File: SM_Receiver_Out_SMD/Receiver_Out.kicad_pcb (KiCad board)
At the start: 2 copper layers, 83.2 x 71.4 mm, 47 parts, among them J1 String1, J2 String2, J3 String3, J4 String4, J5 OLED, J6 VIN_Voltage, J7 RJ45, J8 RJ45, SW1 ID, SW2 Terminators, SW3 User, SW4 RUN, U1 74AHCT1G125, U2 AMS1117-5.0, U3 AM26C32IN, U4 74AHCT1G125, U5 74AHCT1G125, U6 74AHCT1G125, U7 Pico

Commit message: working on BOM
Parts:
- added J10: SWD, Scotts:1x02_Horizontal_SMD, B.Cu at (63.6, 82.9)
- added J9: Debug, Connector_PinHeader_2.54mm:PinHeader_1x03_P2.54mm_Vertical, F.Cu at (70.0, 150.0)
- added R2: 100K, Resistor_SMD:R_0603_1608Metric_Pad0.98x0.95mm_HandSolder, F.Cu at (78.0, 139.0)
- added TP1: DATA1, TestPoint:TestPoint_Pad_D1.5mm, B.Cu at (64.7, 134.7)
- added TP2: DATA2, TestPoint:TestPoint_Pad_D1.5mm, B.Cu at (64.7, 132.1)
- added TP3: DATA3, TestPoint:TestPoint_Pad_D1.5mm, B.Cu at (64.7, 129.5)
- added TP4: DATA4, TestPoint:TestPoint_Pad_D1.5mm, B.Cu at (64.7, 127.0)
- added TP5: EN1, TestPoint:TestPoint_Pad_D1.5mm, B.Cu at (64.6, 109.2)
- added TP6: EN2, TestPoint:TestPoint_Pad_D1.5mm, B.Cu at (64.5, 106.7)
- added TP7: EN3, TestPoint:TestPoint_Pad_D1.5mm, B.Cu at (64.4, 104.2)
- added TP8: EN4, TestPoint:TestPoint_Pad_D1.5mm, B.Cu at (64.4, 101.6)
- moved REF** 3.70 mm to (53.5, 116.9)
- turned D4 to 180 degrees
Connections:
- R11 pad 1: Net-(D4-Pad2) -> Net-(D4-Pad1)
- U3 pad 12: GND -> DIFF_EN
- U7 pad 1: unconnected-(U7-Pad1) -> Net-(J9-Pad2)
- U7 pad 11: unconnected-(U7-Pad11) -> DIFF_EN
- U7 pad 2: unconnected-(U7-Pad2) -> Net-(J9-Pad1)
- U7 pad 41: unconnected-(U7-Pad41) -> /Micro/SWDCLK
- U7 pad 42: unconnected-(U7-Pad42) -> GND
- U7 pad 43: unconnected-(U7-Pad43) -> /Micro/SWDIO
- U7 pad 9: Net-(D4-Pad1) -> Net-(D4-Pad2)
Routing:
- net DIFF_EN: track 0.00 -> 39.1 mm, vias 0 -> 2
- net Net-(D4-Pad2): track 1.91 -> 26.3 mm
- net Net-(D4-Pad1): track 26.3 -> 1.91 mm
- net Net-(J9-Pad1): track 0.00 -> 14.6 mm
- net Net-(J9-Pad2): track 0.00 -> 12.5 mm
- net /Micro/SWDIO: track 0.00 -> 12.5 mm, vias 0 -> 1
- net /Micro/SWDCLK: track 0.00 -> 11.5 mm, vias 0 -> 1
- net EN3: track 10.8 -> 13.5 mm
- net EN4: track 8.43 -> 11.1 mm
- net EN2: track 8.62 -> 11.2 mm
- net EN1: track 9.27 -> 11.8 mm
- net OUT17: track 34.8 -> 37.3 mm
- net OUT18: track 43.9 -> 46.3 mm
- net OUT19: track 36.2 -> 38.6 mm
- net OUT20: track 46.7 -> 49.1 mm
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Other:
- board text added: "${TITLE} ${REVISION} By ${COMPANY}"
- board text added: "GP0"
- board text added: "GP1"
- board text added: "SWDCLK"
- board text added: "SWDIO"
- board text removed: "SM Receiver v1 By Scott Hanson"

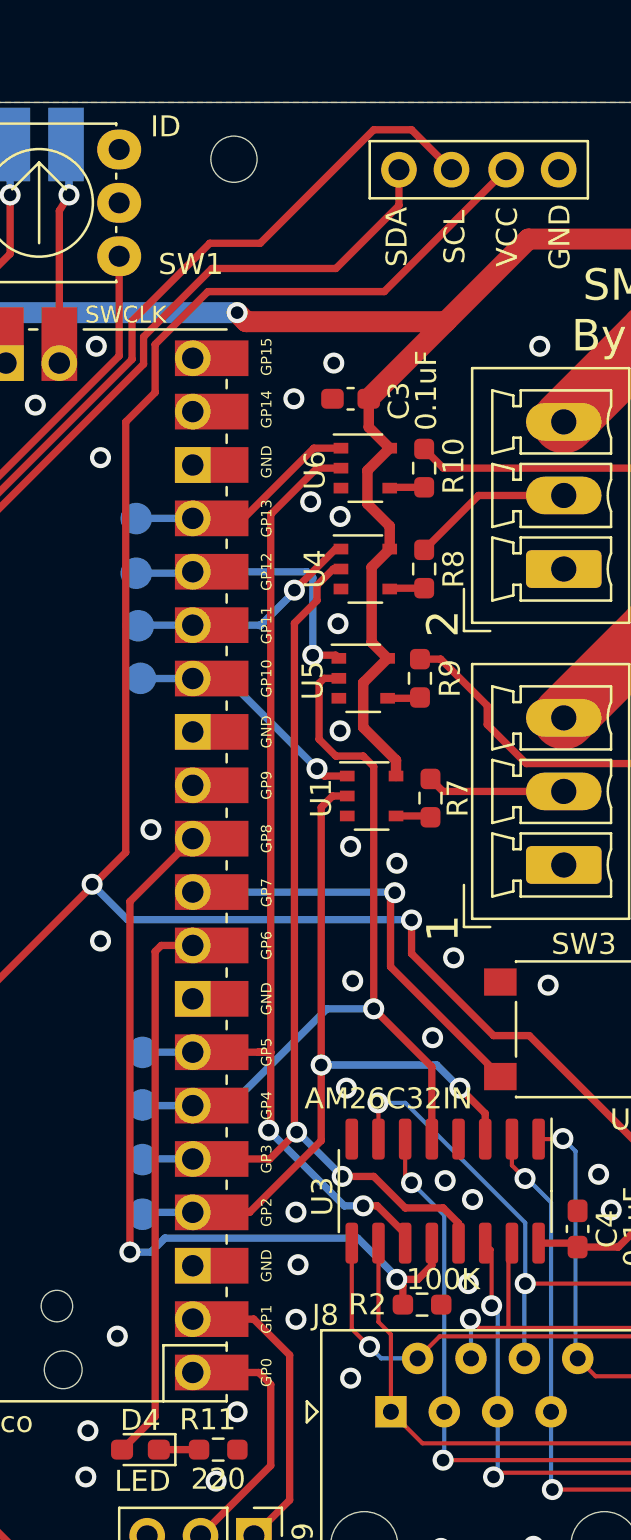
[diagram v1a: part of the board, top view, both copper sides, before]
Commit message: fixing I2C lines were backwards
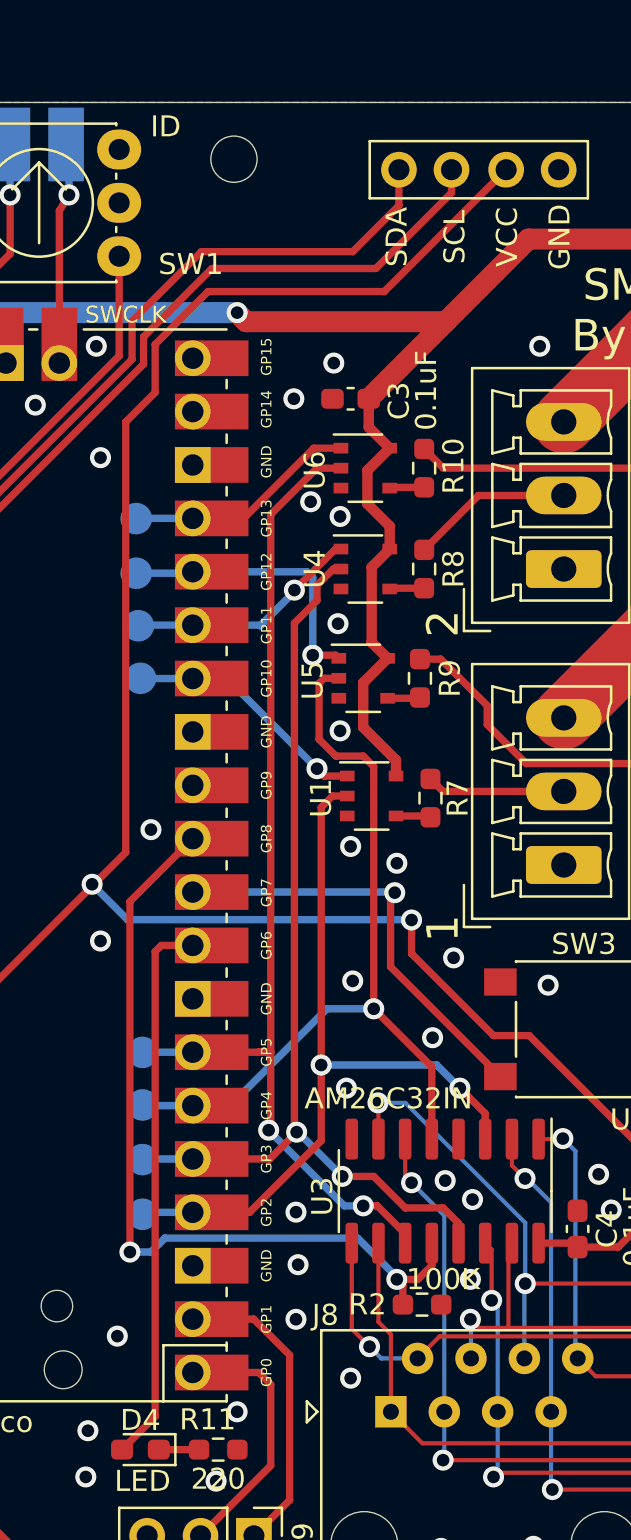
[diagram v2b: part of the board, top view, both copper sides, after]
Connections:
- J5 pad 1: Net-(J5-Pad1) -> /Micro/SDA
- J5 pad 2: Net-(J5-Pad2) -> /Micro/SCL
- U7 pad 31: Net-(J5-Pad2) -> /Micro/SDA
- U7 pad 32: Net-(J5-Pad1) -> /Micro/SCL
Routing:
- net /Micro/SCL: track 0.00 -> 53.9 mm
- net Net-(J5-Pad2): track 53.7 -> 0.00 mm
- net Net-(J5-Pad1): track 51.8 -> 0.00 mm
- net /Micro/SDA: track 0.00 -> 50.6 mm

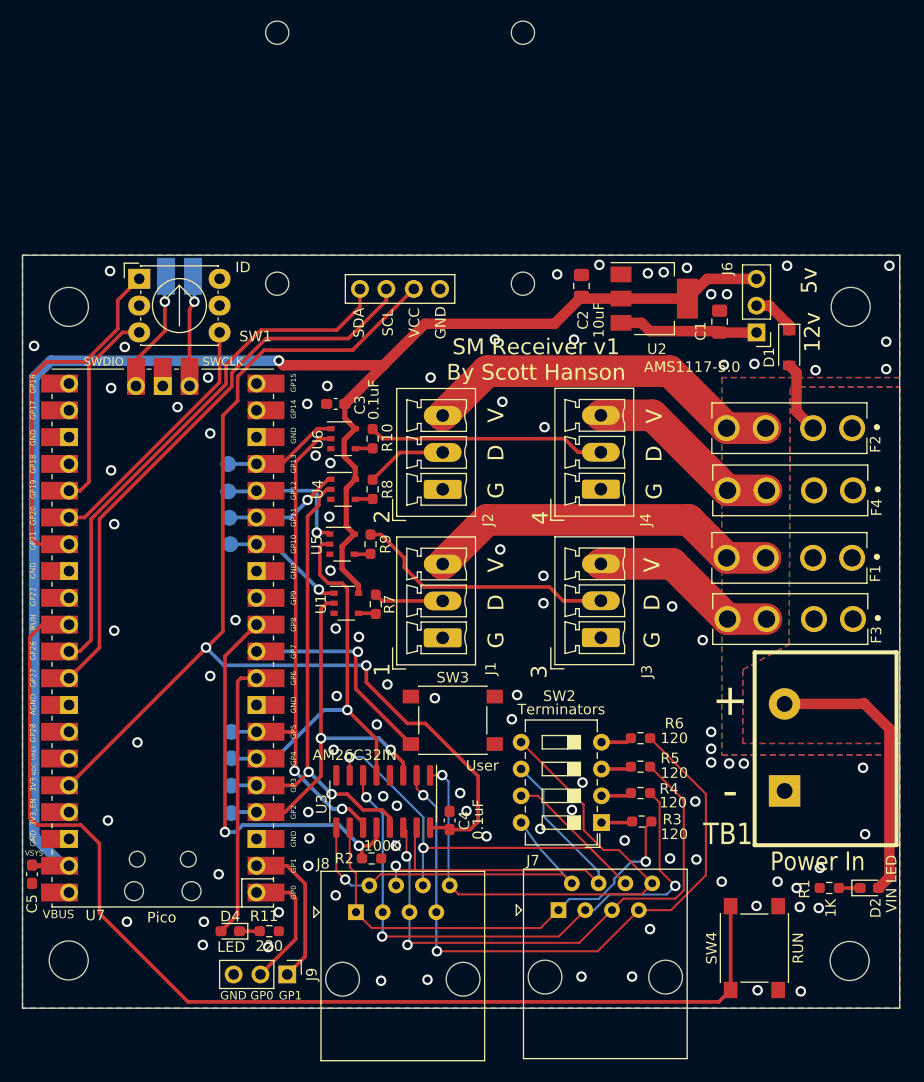
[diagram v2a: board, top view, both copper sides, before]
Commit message: fix miswired serial receiver
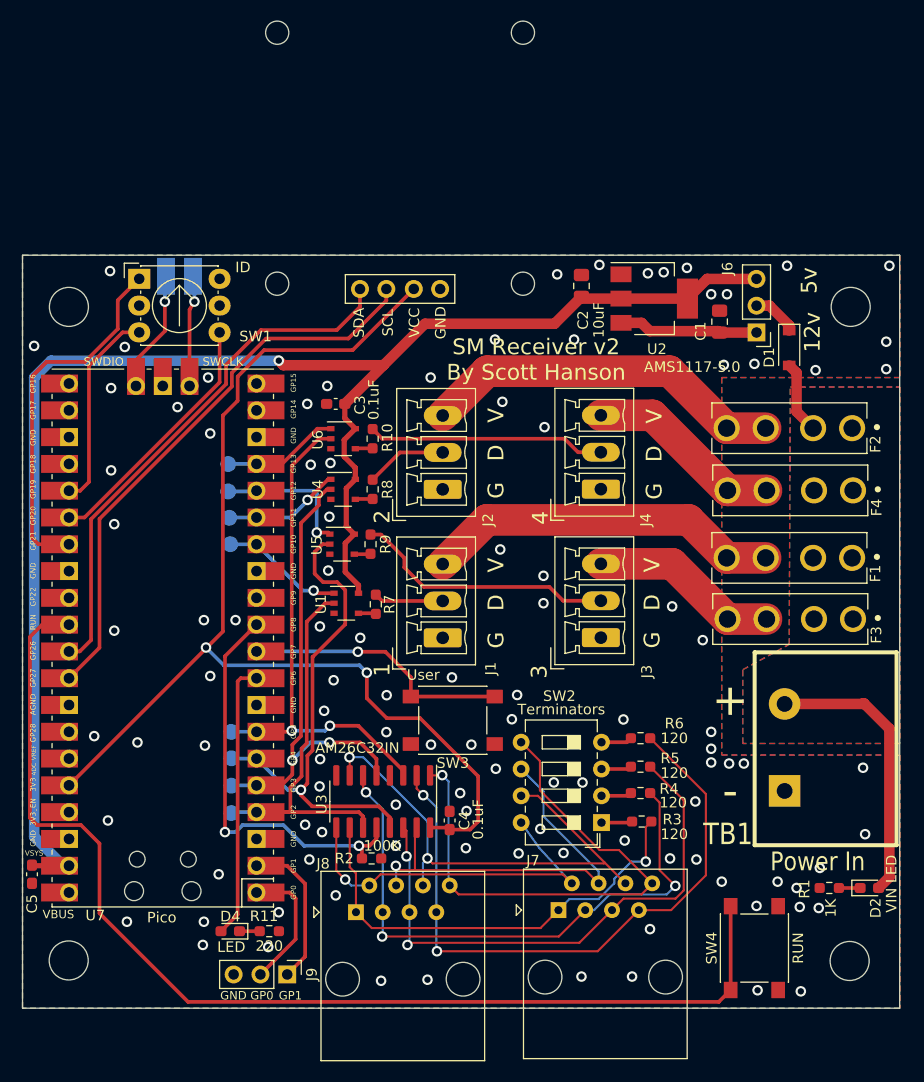
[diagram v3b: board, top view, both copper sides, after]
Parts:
- turned SW3 to 180 degrees
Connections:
- U3 pad 11: OUT20 -> OUT17
- U3 pad 13: OUT18 -> OUT19
- U3 pad 3: OUT17 -> OUT20
- U3 pad 5: OUT19 -> OUT18
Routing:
- net OUT19: track 38.6 -> 46.6 mm
- net Net-(SW3-Pad2): track 20.6 -> 25.7 mm
- net OUT17: track 37.3 -> 39.0 mm, vias 2 -> 0
- net GND: track 0.00 -> 0.15 mm, vias 97 -> 107

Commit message: added 100 ohms to lines
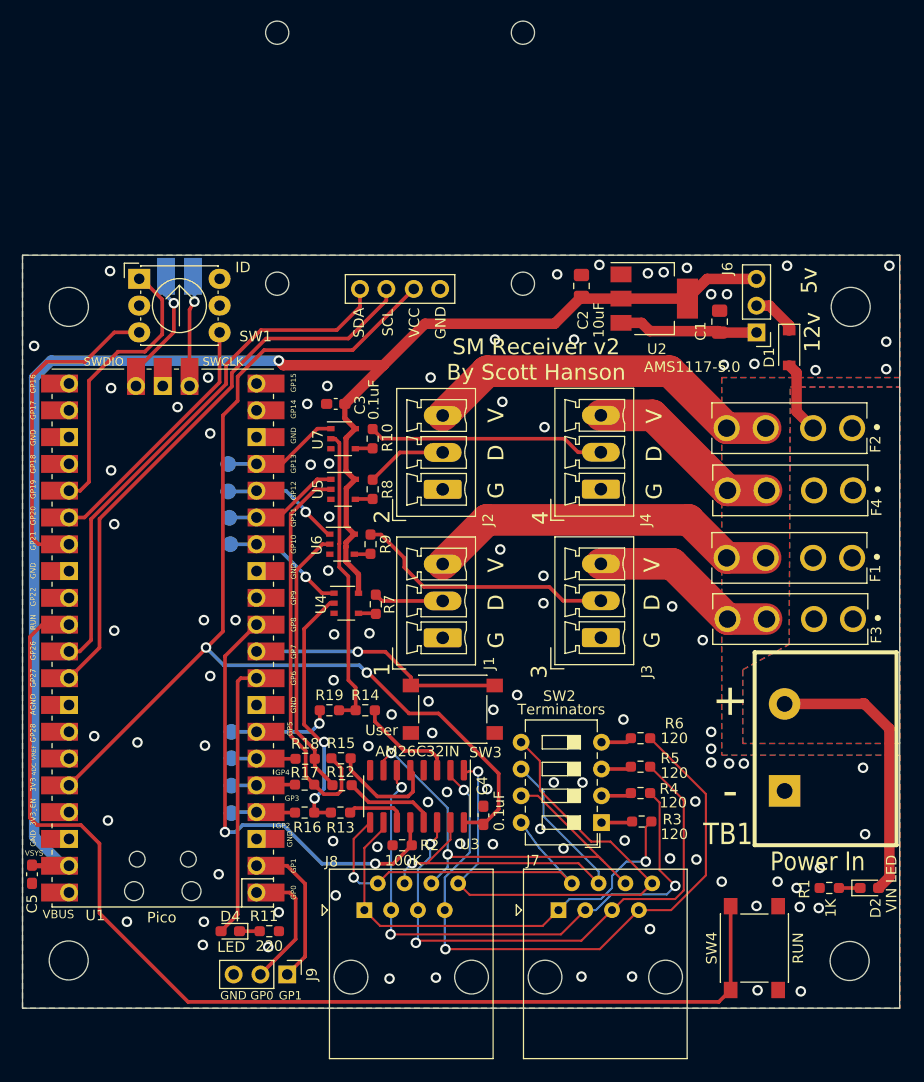
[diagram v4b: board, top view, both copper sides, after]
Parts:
- added R12: 100ohm, Resistor_SMD:R_0603_1608Metric_Pad0.98x0.95mm_HandSolder, F.Cu at (75.2, 132.1)
- added R13: 100ohm, Resistor_SMD:R_0603_1608Metric_Pad0.98x0.95mm_HandSolder, F.Cu at (75.1, 134.7)
- added R14: 100ohm, Resistor_SMD:R_0603_1608Metric_Pad0.98x0.95mm_HandSolder, F.Cu at (77.4, 125.0)
- added R15: 100ohm, Resistor_SMD:R_0603_1608Metric_Pad0.98x0.95mm_HandSolder, F.Cu at (75.1, 129.5)
- added R16: 100ohm, Resistor_SMD:R_0603_1608Metric_Pad0.98x0.95mm_HandSolder, F.Cu at (71.7, 134.7)
- added R17: 100ohm, Resistor_SMD:R_0603_1608Metric_Pad0.98x0.95mm_HandSolder, F.Cu at (71.7, 132.0)
- added R18: 100ohm, Resistor_SMD:R_0603_1608Metric_Pad0.98x0.95mm_HandSolder, F.Cu at (71.7, 129.6)
- added R19: 100ohm, Resistor_SMD:R_0603_1608Metric_Pad0.98x0.95mm_HandSolder, F.Cu at (74.0, 125.0)
- moved C4 3.24 mm to (88.6, 134.9)
- moved U3 3.24 mm to (82.3, 133.1)
- moved R2 3.16 mm to (80.9, 137.8), turned to 180 degrees
- moved SW3 1.05 mm to (85.7, 124.9)
- moved J8 0.82 mm to (77.3, 143.9)
- renumbered U7 to U1, U1 to U4, U4 to U5, U5 to U6, U6 to U7
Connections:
- TP1 pad 1: OUT17 -> Net-(R16-Pad1)
- TP2 pad 1: OUT18 -> Net-(R17-Pad1)
- TP3 pad 1: OUT19 -> Net-(R18-Pad1)
- TP4 pad 1: OUT20 -> Net-(R19-Pad1)
- U1 pad 25: Net-(SW1-Pad4) -> Net-(SW1-Pad1)
- U1 pad 27: Net-(SW1-Pad1) -> Net-(SW1-Pad4)
- U1 pad 4: OUT17 -> Net-(R16-Pad1)
- U1 pad 5: OUT18 -> Net-(R17-Pad1)
- U1 pad 6: OUT19 -> Net-(R18-Pad1)
- U1 pad 7: OUT20 -> Net-(R19-Pad1)
- U3 pad 11: OUT17 -> Net-(R13-Pad1)
- U3 pad 13: OUT19 -> Net-(R12-Pad1)
- U3 pad 3: OUT20 -> Net-(R14-Pad2)
- U3 pad 5: OUT18 -> Net-(R15-Pad2)
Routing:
- net OUT19: track 46.6 -> 26.0 mm, vias 1 -> 0
- net OUT20: track 48.7 -> 28.5 mm, vias 2 -> 0
- net OUT17: track 39.0 -> 24.2 mm, vias 0 -> 2
- net Net-(SW1-Pad4): track 19.3 -> 31.0 mm
- net Net-(R15-Pad2): track 0.00 -> 10.4 mm
- net Net-(R19-Pad1): track 0.00 -> 9.95 mm, vias 0 -> 1
- net Net-(R14-Pad2): track 0.00 -> 9.59 mm
- net Net-(R12-Pad1): track 0.00 -> 8.82 mm
- net OUT18: track 45.9 -> 37.9 mm, vias 2 -> 0
- net Net-(SW1-Pad1): track 34.7 -> 26.9 mm
- net Net-(R18-Pad1): track 0.00 -> 6.11 mm
- net Net-(R16-Pad1): track 0.00 -> 6.09 mm
- net Net-(R17-Pad1): track 0.00 -> 6.08 mm
- net Net-(R13-Pad1): track 0.00 -> 5.78 mm
- net DIFF_EN: track 39.0 -> 43.4 mm
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
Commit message: i think Kicad has a bug
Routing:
- net Serial2_N: track 45.5 -> 46.1 mm
